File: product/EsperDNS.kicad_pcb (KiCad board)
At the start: 2 copper layers, 45.1 x 83.7 mm, 61 parts, among them J1 10118192-0001LF, J2 ARJM11A3, J3 Conn_02x05_Odd_Even, Q1 Q_NMOS_GSD, Q2 Q_NMOS_GSD, Q3 Q_NMOS_GSD, U1 AZ1117-3.3, U2 LAN8720A, U3 ESP32-WROOM-32D, X1 ECS-2520MV

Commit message: Added first revision of programmer board
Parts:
- R25, R26: value 10 -> 33
- renumbered YLW to D3, RED to D4, BLUE to D5, BLOCK to SW1, PWR to SW2
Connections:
- net +5V renamed Net-(J3-Pad1)
- J3 pad 10: Net-(J3-Pad10) -> GND
- J3 pad 9: GND -> Net-(J3-Pad9)

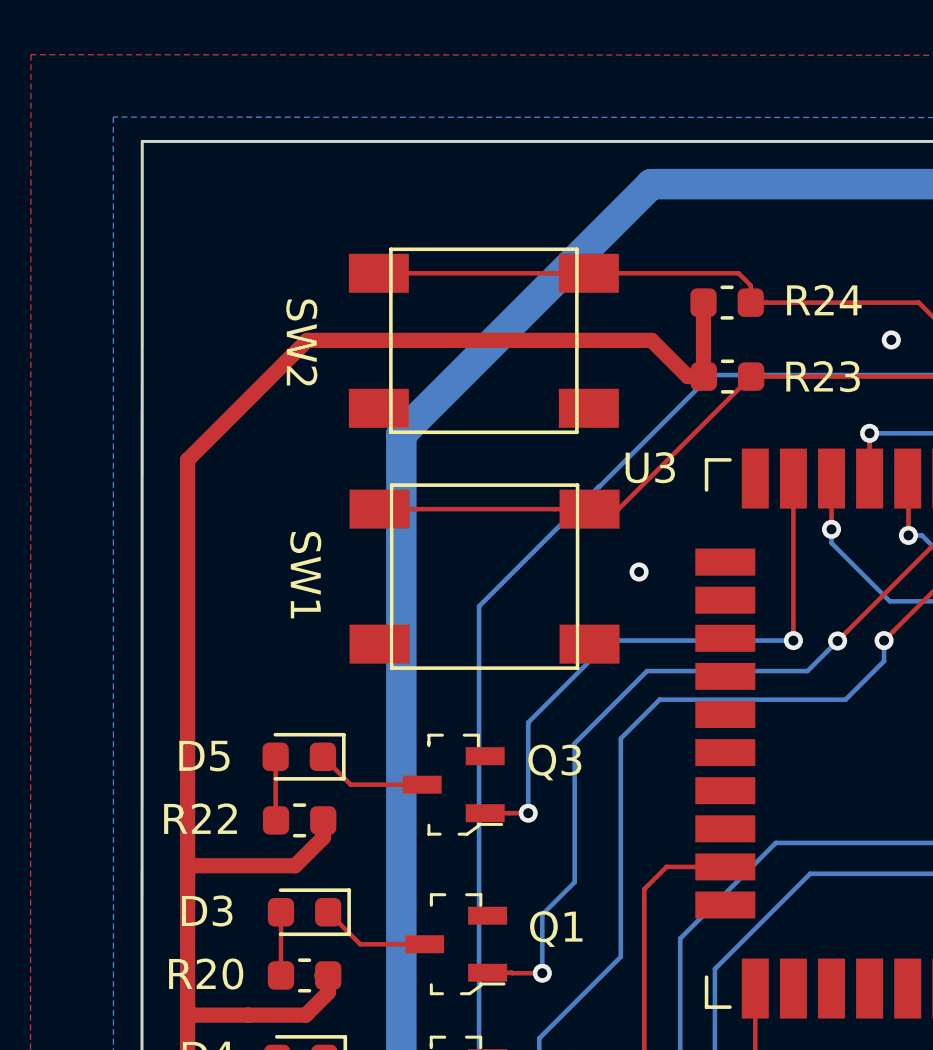
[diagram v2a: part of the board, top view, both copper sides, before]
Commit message: Added LCSC part numbers for product board
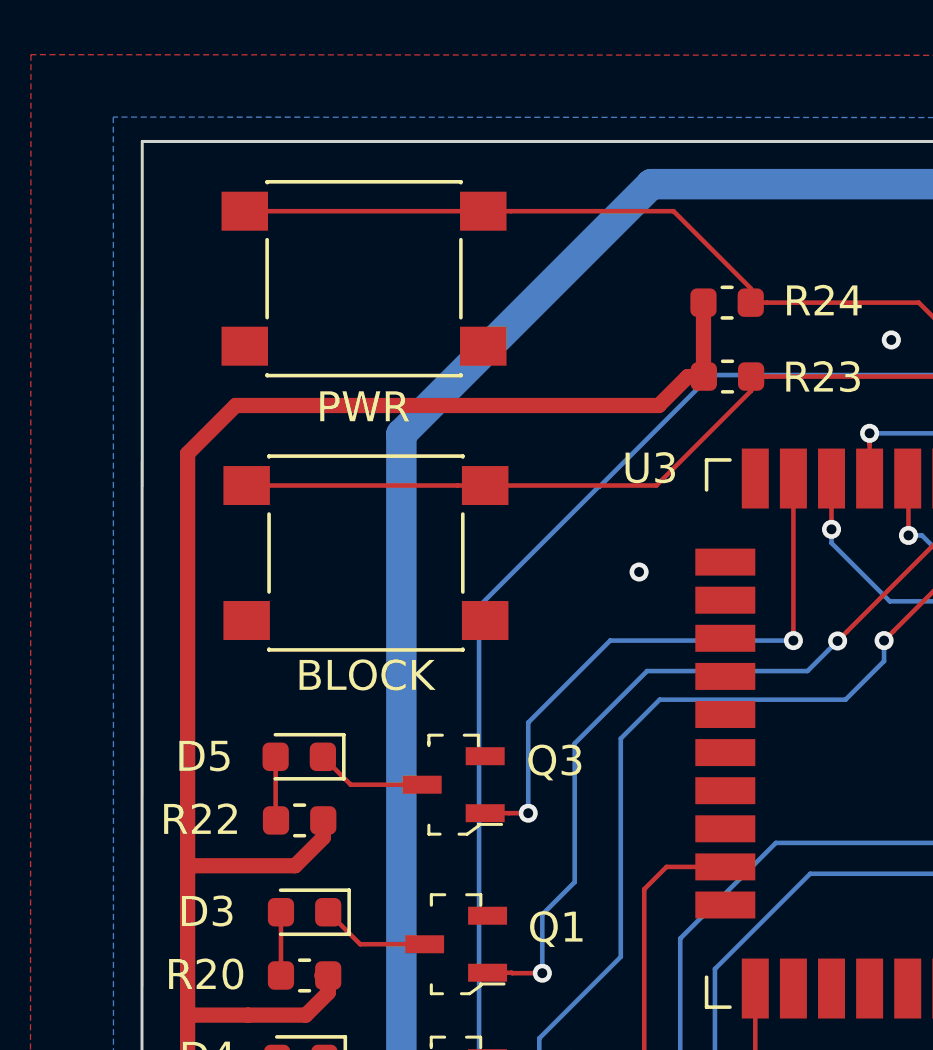
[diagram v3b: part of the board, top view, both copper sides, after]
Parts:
- SW1, SW2: value 222CMVBAR -> SW_SPST; footprint My Footprints:222CMVBAR -> Button_Switch_SMD:SW_Push_1P1T_NO_6x6mm_H9.5mm
- moved SW2 4.50 mm to (124.0, 60.5)
- moved SW1 4.03 mm to (124.1, 69.7)
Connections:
- SW1 pad 2: GND -> BLOCK
- SW2 pad 2: GND -> RESTART
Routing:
- net RESTART: track 26.6 -> 31.8 mm
- net BLOCK: track 25.0 -> 29.4 mm
- net VBUS: track 116.8 -> 116.0 mm
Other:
- board text added: "BLOCK"
- board text added: "PWR"

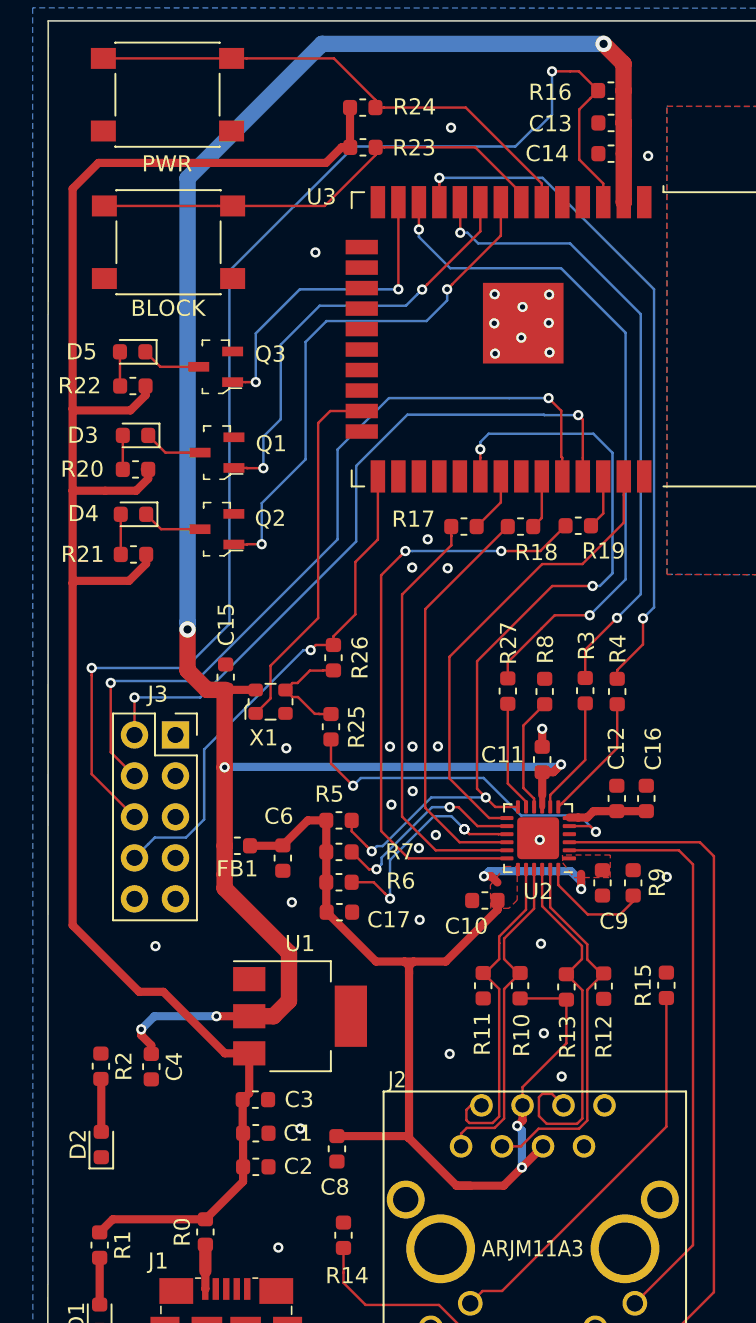
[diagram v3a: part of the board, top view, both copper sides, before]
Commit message: Swapped TX & RX on Product Board
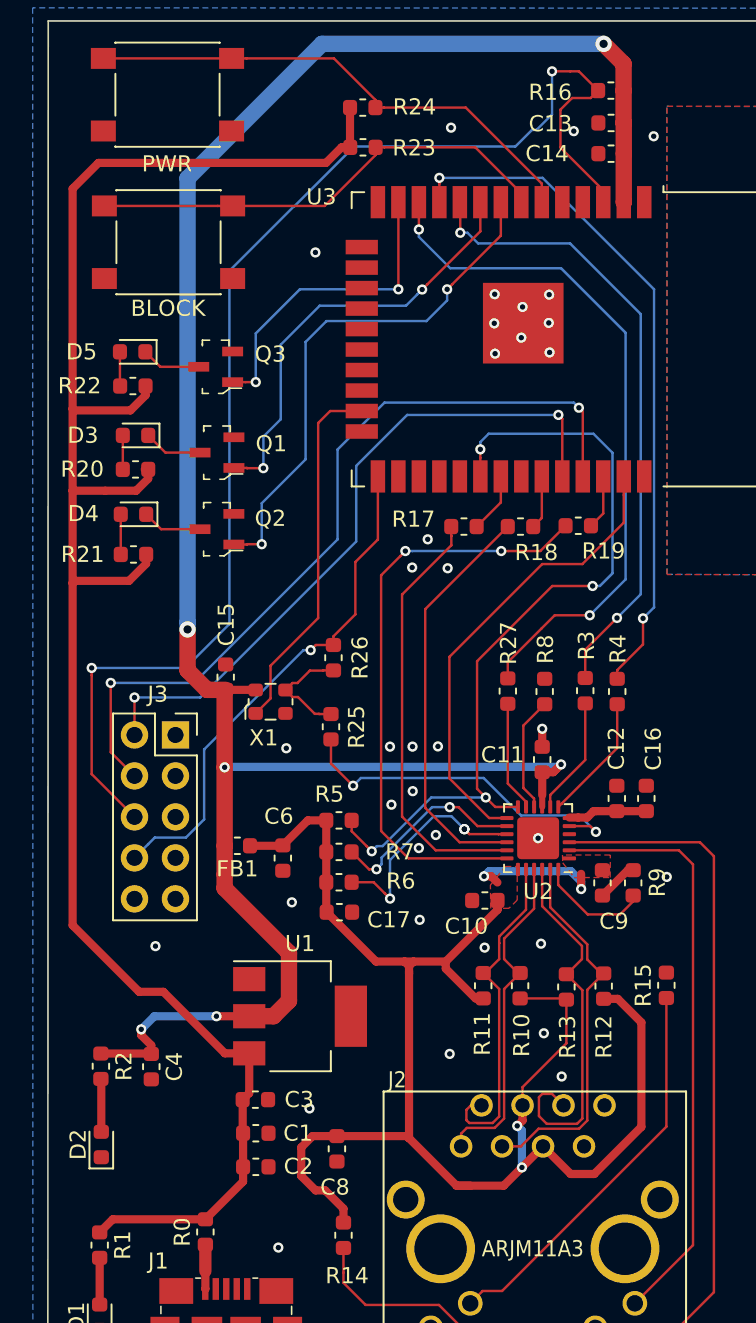
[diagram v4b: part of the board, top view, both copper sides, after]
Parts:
- D1, D2: value LED -> GRN
- D3: value LED -> YLW
- D4: value LED -> RED
- D5: value LED -> BLUE
- R17, R18, R19: value 10 -> 100
- R27, R3, R4: value 10K -> 100
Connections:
- R27 pad 1: CRS_DV -> /Page 1/CRS_DV
- R27 pad 2: CRS_DV -> CRS_DV_r
- U2 pad 11: CRS_DV -> /Page 1/CRS_DV
- U3 pad 12: CRS_DV -> CRS_DV_r
- U3 pad 34: RX -> TX
- U3 pad 35: TX -> RX
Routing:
- net CRS_DV: track 50.0 -> 0.00 mm, vias 2 -> 0
- net CRS_DV_r: track 0.00 -> 43.1 mm, vias 0 -> 2
- net AVDD: track 76.0 -> 106.0 mm
- net /Page 1/CRS_DV: track 0.00 -> 6.86 mm
- net +3V3: track 131.9 -> 135.0 mm
- net GND: track 1.12 -> 3.67 mm, vias 35 -> 37
- net EN: track 79.9 -> 81.6 mm
- net TX: track 43.8 -> 42.5 mm
- net RX: track 49.3 -> 50.3 mm

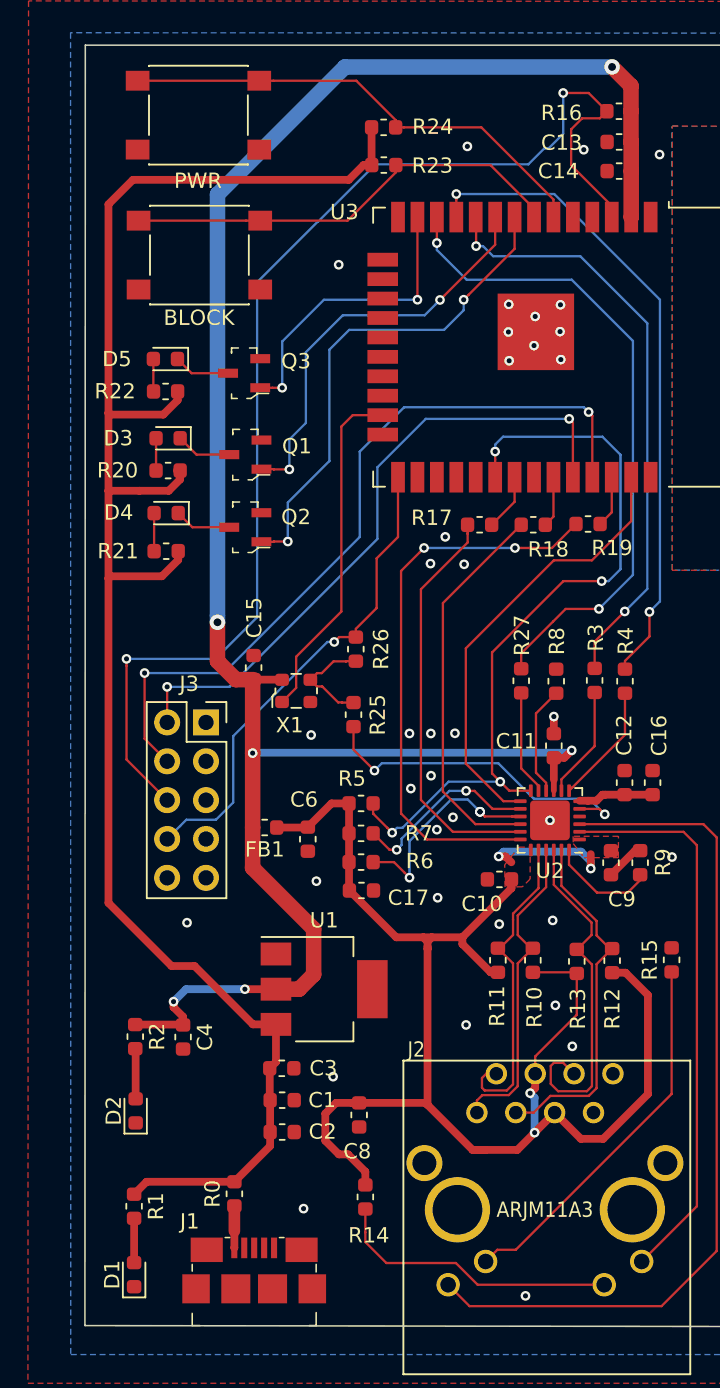
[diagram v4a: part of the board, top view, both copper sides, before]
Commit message: Moved connector and added silkscreen labels on product board
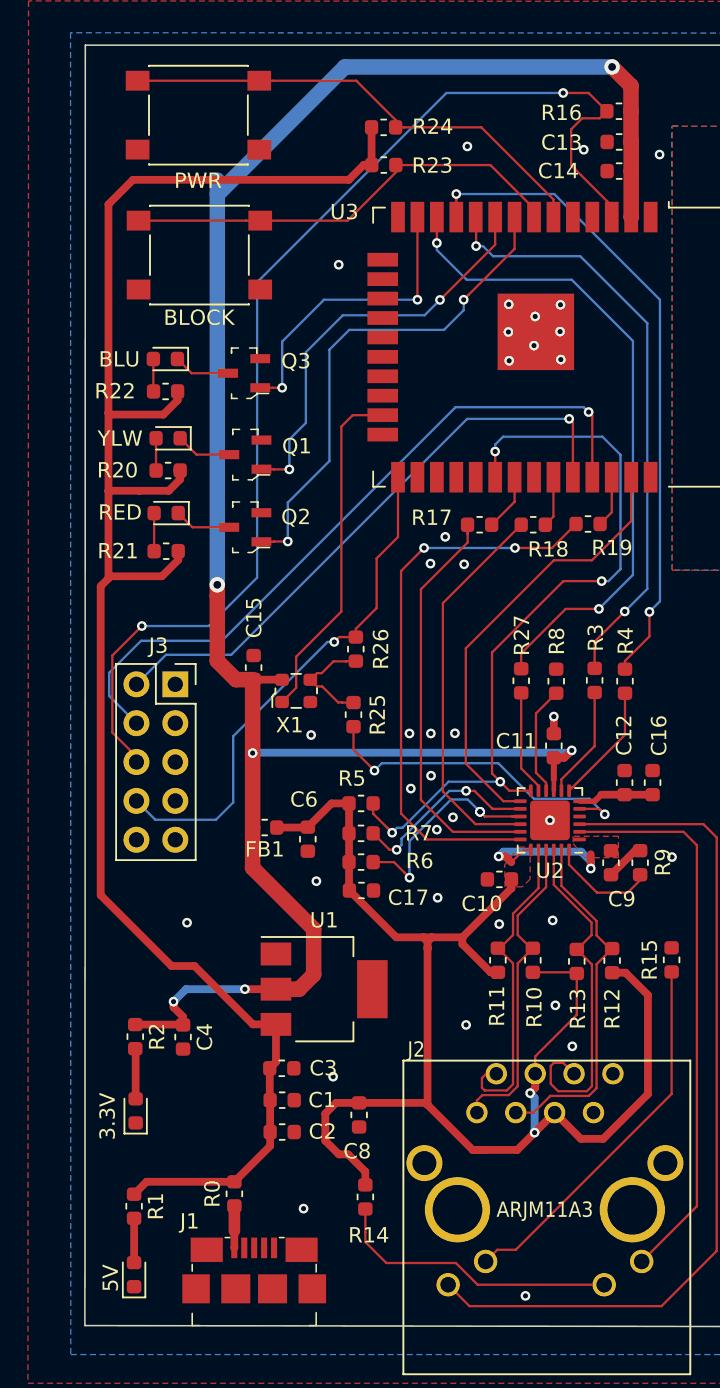
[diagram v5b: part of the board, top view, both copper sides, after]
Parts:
- moved J3 3.20 mm to (122.5, 97.7)
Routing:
- net EN: track 81.6 -> 76.8 mm
- net RX: track 50.3 -> 47.0 mm, vias 2 -> 1
- net TX: track 42.5 -> 39.4 mm, vias 2 -> 1
- net BOOTMODE: track 31.9 -> 33.9 mm
- net AVDD: track 106.0 -> 107.6 mm
- net +3V3: track 135.0 -> 136.0 mm
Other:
- board text added: "3.3V"
- board text added: "5V"
- board text added: "BLU"
- board text added: "RED"
- board text added: "YLW"

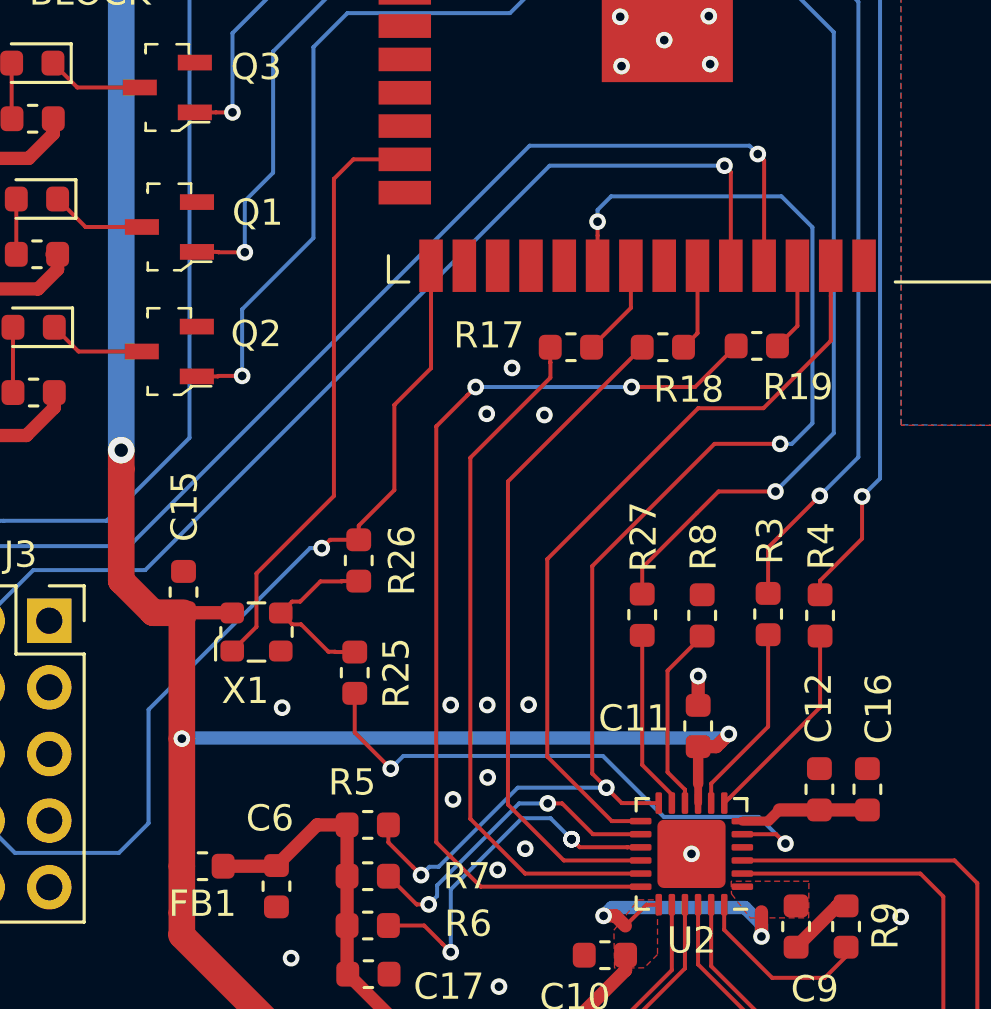
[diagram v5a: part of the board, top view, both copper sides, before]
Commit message: Removed oscillator, replaced with IO17
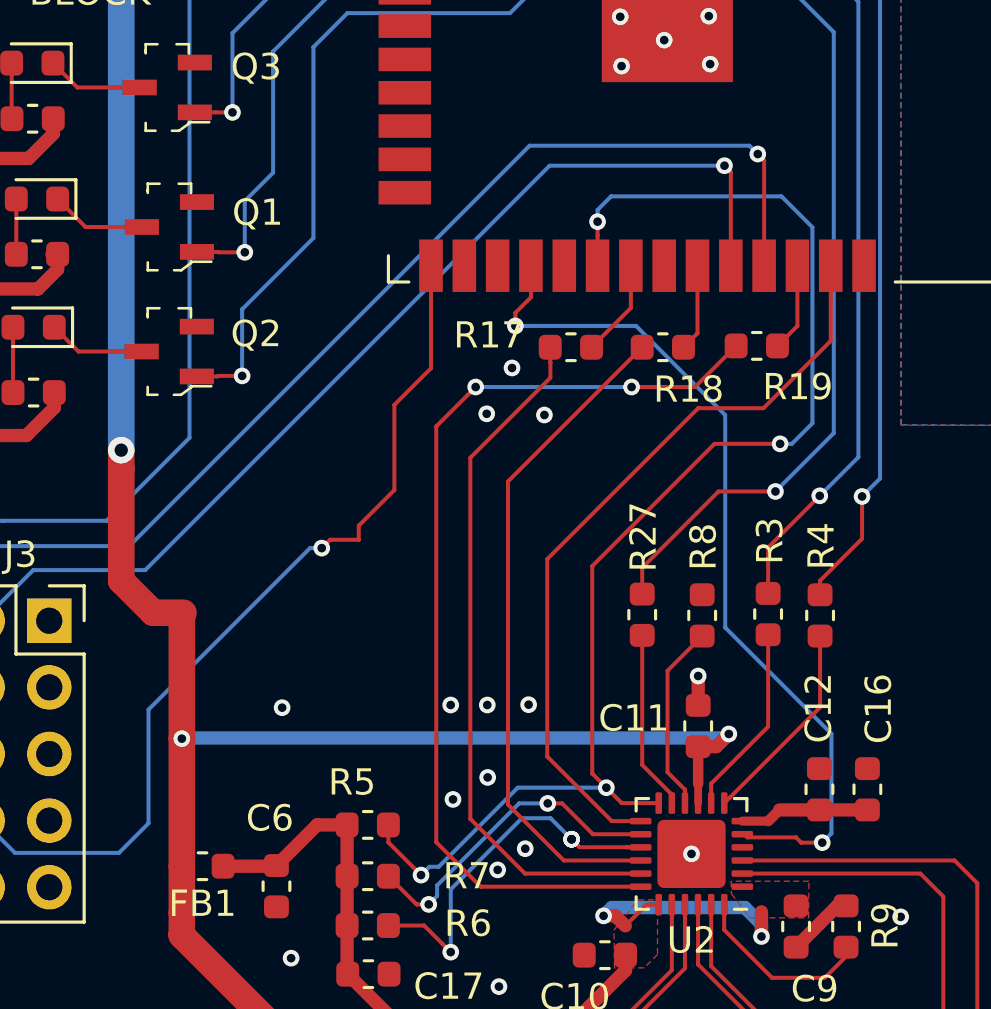
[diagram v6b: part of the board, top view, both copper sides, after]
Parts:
- removed C15: 0.1uF, Capacitor_SMD:C_0603_1608Metric
- removed R25, R26: 33, Resistor_SMD:R_0603_1608Metric
- removed X1: ECS-2520MV, Oscillator:Oscillator_SMD_ECS_2520MV-xxx-xx-4Pin_2.5x2.0mm
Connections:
- U2 pad 5: CLKIN -> CLK50MHZ
- U3 pad 28: Net-(U3-Pad28) -> CLK50MHZ
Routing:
- net CLK50MHZ: track 0.00 -> 33.3 mm, vias 0 -> 2
- net CLKEN: track 22.6 -> 0.00 mm
- net CLKIN: track 22.2 -> 0.00 mm, vias 2 -> 0
- net Net-(R25-Pad1): track 6.91 -> 0.00 mm
- net +3V3: track 136.0 -> 134.1 mm
